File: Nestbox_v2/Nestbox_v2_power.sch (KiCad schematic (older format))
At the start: 24 parts, among them J201 BATT_CONN_01X02, U201 TPS62745, U202 LTC3534, U203 LP5907

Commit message: added stitching vias at power stage; reverse polarity protection and SD car enable mosfet
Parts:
- added Q201: Q_PMOS_DGS, Octanis3:TDSON-8-1_HandSoldering, symbol Q_PMOS_DGS
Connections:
- net +BATT: now also Q201.3 (S); no longer J201.2 (P2)
- net GND: now also U201.GND1 (GND), U201.GND2 (GND), Q201.2 (G)
- new net batt_in: J201.2 (P2), Q201.1 (D)
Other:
- moved on the sheet: J201
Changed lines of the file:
@@
 $EndComp
 $Comp
-L GND #PWR01
+L GND #PWR208
 U 1 1 5A0217A9
 P 3000 2550
-F 0 "#PWR01" H 3000 2300 50  0001 C CNN
+F 0 "#PWR208" H 3000 2300 50  0001 C CNN
 F 1 "GND" H 3005 2377 50  0000 C CNN
 F 2 "" H 3000 2550 50  0001 C CNN
@@
 $EndComp
 $Comp
-L GND #PWR02
+L GND #PWR203
 U 1 1 5A021A75
 P 1750 2400
-F 0 "#PWR02" H 1750 2150 50  0001 C CNN
+F 0 "#PWR203" H 1750 2150 50  0001 C CNN
 F 1 "GND" H 1755 2227 50  0000 C CNN
 F 2 "" H 1750 2400 50  0001 C CNN
@@
 $EndComp
 $Comp
-L +3.3V #PWR03
+L +3.3V #PWR219
 U 1 1 5A021DFB
 P 6750 1900
-F 0 "#PWR03" H 6750 1750 50  0001 C CNN
+F 0 "#PWR219" H 6750 1750 50  0001 C CNN
 F 1 "+3.3V" V 6765 2028 50  0000 L CNN
 F 2 "" H 6750 1900 50  0001 C CNN
@@
 $EndComp
 $Comp
-L GND #PWR04
+L GND #PWR209
 U 1 1 5A022A31
 P 3000 4850
-F 0 "#PWR04" H 3000 4600 50  0001 C CNN
+F 0 "#PWR209" H 3000 4600 50  0001 C CNN
 F 1 "GND" H 3005 4677 50  0000 C CNN
 F 2 "" H 3000 4850 50  0001 C CNN
@@
 $EndComp
 $Comp
-L GND #PWR05
+L GND #PWR205
 U 1 1 5A022A41
 P 2150 4650
-F 0 "#PWR05" H 2150 4400 50  0001 C CNN
+F 0 "#PWR205" H 2150 4400 50  0001 C CNN
 F 1 "GND" H 2155 4477 50  0000 C CNN
 F 2 "" H 2150 4650 50  0001 C CNN
@@
 $EndComp
 $Comp
-L +5V #PWR06
+L +5V #PWR220
 U 1 1 5A0232FE
 P 7600 4150
-F 0 "#PWR06" H 7600 4000 50  0001 C CNN
+F 0 "#PWR220" H 7600 4000 50  0001 C CNN
 F 1 "+5V" V 7615 4278 50  0000 L CNN
 F 2 "" H 7600 4150 50  0001 C CNN
@@
 $EndComp
 $Comp
-L GND #PWR07
+L GND #PWR218
 U 1 1 5A0246BF
 P 6500 4700
-F 0 "#PWR07" H 6500 4450 50  0001 C CNN
+F 0 "#PWR218" H 6500 4450 50  0001 C CNN
 F 1 "GND" H 6505 4527 50  0000 C CNN
 F 2 "" H 6500 4700 50  0001 C CNN
@@
 $EndComp
 $Comp
-L GND #PWR08
+L GND #PWR217
 U 1 1 5A0247CA
 P 5650 4800
-F 0 "#PWR08" H 5650 4550 50  0001 C CNN
+F 0 "#PWR217" H 5650 4550 50  0001 C CNN
 F 1 "GND" H 5655 4627 50  0000 C CNN
 F 2 "" H 5650 4800 50  0001 C CNN
@@
 $EndComp
 $Comp
-L GND #PWR09
+L GND #PWR216
 U 1 1 5A024E9A
 P 5300 2400
-F 0 "#PWR09" H 5300 2150 50  0001 C CNN
+F 0 "#PWR216" H 5300 2150 50  0001 C CNN
 F 1 "GND" H 5305 2227 50  0000 C CNN
 F 2 "" H 5300 2400 50  0001 C CNN
@@
 L CONN_01X02 J201
 U 1 1 5B072802
-P 8850 3200
-F 0 "J201" H 8850 3350 50  0000 C CNN
-F 1 "BATT_CONN_01X02" V 8950 3200 50  0000 C CNN
-F 2 "Terminal_Blocks:TerminalBlock_Pheonix_PT-3.5mm_2pol" H 8850 3200 50  0001 C CNN
-F 3 "" H 8850 3200 50  0001 C CNN
-	1    8850 3200
-	1    0    0    -1
-$EndComp
-$Comp
-L GND #PWR010
+P 9550 3200
+F 0 "J201" H 9550 3350 50  0000 C CNN
+F 1 "BATT_CONN_01X02" V 9650 3200 50  0000 C CNN
+F 2 "Terminal_Blocks:TerminalBlock_Pheonix_PT-3.5mm_2pol" H 9550 3200 50  0001 C CNN
+F 3 "" H 9550 3200 50  0001 C CNN
+	1    9550 3200
+	1    0    0    -1
+$EndComp
+$Comp
+L GND #PWR222
 U 1 1 5B072B3F
 P 8350 3150
-F 0 "#PWR010" H 8350 2900 50  0001 C CNN
+F 0 "#PWR222" H 8350 2900 50  0001 C CNN
 F 1 "GND" H 8350 3000 50  0000 C CNN
 F 2 "" H 8350 3150 50  0001 C CNN
@@
 $EndComp
 $Comp
-L +3V3 #PWR011
+L +3V3 #PWR204
 U 1 1 5B0757C4
 P 1950 6350
-F 0 "#PWR011" H 1950 6200 50  0001 C CNN
+F 0 "#PWR204" H 1950 6200 50  0001 C CNN
 F 1 "+3V3" H 1965 6523 50  0000 C CNN
 F 2 "" H 1950 6350 50  0001 C CNN
@@
 $EndComp
 $Comp
-L GND #PWR012
+L GND #PWR211
 U 1 1 5B0757CA
 P 3600 6800
-F 0 "#PWR012" H 3600 6550 50  0001 C CNN
+F 0 "#PWR211" H 3600 6550 50  0001 C CNN
 F 1 "GND" H 3605 6627 50  0000 C CNN
 F 2 "" H 3600 6800 50  0001 C CNN
@@
 NoConn ~ 4100 6450
 $Comp
-L VAA #PWR013
+L VAA #PWR215
 U 1 1 5B0757D1
 P 4700 5750
-F 0 "#PWR013" H 4700 5600 50  0001 C CNN
+F 0 "#PWR215" H 4700 5600 50  0001 C CNN
 F 1 "VAA" H 4717 5923 50  0000 C CNN
 F 2 "" H 4700 5750 50  0001 C CNN
@@
 $EndComp
 $Comp
-L +BATT #PWR014
+L +BATT #PWR201
 U 1 1 5B09033A
 P 700 1900
-F 0 "#PWR014" H 700 1750 50  0001 C CNN
+F 0 "#PWR201" H 700 1750 50  0001 C CNN
 F 1 "+BATT" H 700 2040 50  0000 C CNN
 F 2 "" H 700 1900 50  0001 C CNN
@@
 $EndComp
 $Comp
-L +BATT #PWR015
+L +BATT #PWR202
 U 1 1 5B090391
 P 1300 4150
-F 0 "#PWR015" H 1300 4000 50  0001 C CNN
+F 0 "#PWR202" H 1300 4000 50  0001 C CNN
 F 1 "+BATT" H 1300 4290 50  0000 C CNN
 F 2 "" H 1300 4150 50  0001 C CNN
@@
 $EndComp
 $Comp
-L GND #PWR016
+L GND #PWR207
 U 1 1 5B090D04
 P 2550 2950
-F 0 "#PWR016" H 2550 2700 50  0001 C CNN
+F 0 "#PWR207" H 2550 2700 50  0001 C CNN
 F 1 "GND" H 2555 2777 50  0000 C CNN
 F 2 "" H 2550 2950 50  0001 C CNN
@@
 $EndComp
 $Comp
-L GND #PWR017
+L GND #PWR206
 U 1 1 5B095296
 P 2500 6850
-F 0 "#PWR017" H 2500 6600 50  0001 C CNN
+F 0 "#PWR206" H 2500 6600 50  0001 C CNN
 F 1 "GND" H 2505 6677 50  0000 C CNN
 F 2 "" H 2500 6850 50  0001 C CNN
@@
 $EndComp
 $Comp
-L GND #PWR018
+L GND #PWR212
 U 1 1 5B095588
 P 4400 6800
-F 0 "#PWR018" H 4400 6550 50  0001 C CNN
+F 0 "#PWR212" H 4400 6550 50  0001 C CNN
 F 1 "GND" H 4405 6627 50  0000 C CNN
 F 2 "" H 4400 6800 50  0001 C CNN
@@
 $EndComp
 $Comp
-L +BATT #PWR019
+L +BATT #PWR221
 U 1 1 5B0B9A8C
 P 8200 3250
-F 0 "#PWR019" H 8200 3100 50  0001 C CNN
+F 0 "#PWR221" H 8200 3100 50  0001 C CNN
 F 1 "+BATT" H 8200 3390 50  0000 C CNN
 F 2 "" H 8200 3250 50  0001 C CNN
@@
 	2900 1900 2900 1700
 Wire Wire Line
-	8650 3150 8350 3150
-Wire Wire Line
-	8200 3250 8650 3250
+	8350 3150 8850 3150
+Wire Wire Line
+	8200 3250 8800 3250
 Wire Wire Line
 	1950 6350 3100 6350
@@
 Connection ~ 4550 4450
 $Comp
-L GND #PWR020
+L GND #PWR213
 U 1 1 5B11A0A6
 P 4500 4900
-F 0 "#PWR020" H 4500 4650 50  0001 C CNN
+F 0 "#PWR213" H 4500 4650 50  0001 C CNN
 F 1 "GND" H 4505 4727 50  0000 C CNN
 F 2 "" H 4500 4900 50  0001 C CNN
@@
 	3000 2400 3050 2400
 $Comp
-L +BATT #PWR021
+L +BATT #PWR214
 U 1 1 5B14A10E
 P 4550 2100
-F 0 "#PWR021" H 4550 1950 50  0001 C CNN
+F 0 "#PWR214" H 4550 1950 50  0001 C CNN
 F 1 "+BATT" H 4550 2240 50  0000 C CNN
 F 2 "" H 4550 2100 50  0001 C CNN
@@
 Wire Wire Line
 	4600 3800 4450 3800
-Connection ~ 8400 3250
 NoConn ~ 4450 1700
+Wire Wire Line
+	3500 2800 3500 2850
+Wire Wire Line
+	3500 2850 3600 2850
+Wire Wire Line
+	3600 2850 3600 2800
+$Comp
+L GND #PWR210
+U 1 1 5B18018D
+P 3500 2850
+F 0 "#PWR210" H 3500 2600 50  0001 C CNN
+F 1 "GND" H 3505 2677 50  0000 C CNN
+F 2 "" H 3500 2850 50  0001 C CNN
+F 3 "" H 3500 2850 50  0001 C CNN
+	1    3500 2850
+	1    0    0    -1
+$EndComp
+$Comp
+L Q_PMOS_DGS Q201
+U 1 1 5B18086E
+P 9000 3150
+F 0 "Q201" H 9200 3200 50  0000 L CNN
+F 1 "Q_PMOS_DGS" H 9200 3100 50  0000 L CNN
+F 2 "Octanis3:TDSON-8-1_HandSoldering" H 9200 3250 50  0001 C CNN
+F 3 "" H 9000 3150 50  0001 C CNN
+	1    9000 3150
+	0    1    1    0
+$EndComp
+Wire Wire Line
+	9200 3250 9350 3250
+Wire Wire Line
+	8850 3150 8850 2900
+Wire Wire Line
+	8850 2900 9250 2900
+Wire Wire Line
+	9250 2900 9250 3150
+Wire Wire Line
+	9250 3150 9350 3150
+Wire Wire Line
+	9000 2950 9000 2900
+Connection ~ 9000 2900
+Text Label 9200 3250 0    60   ~ 0
+batt_in
 $EndSCHEMATC

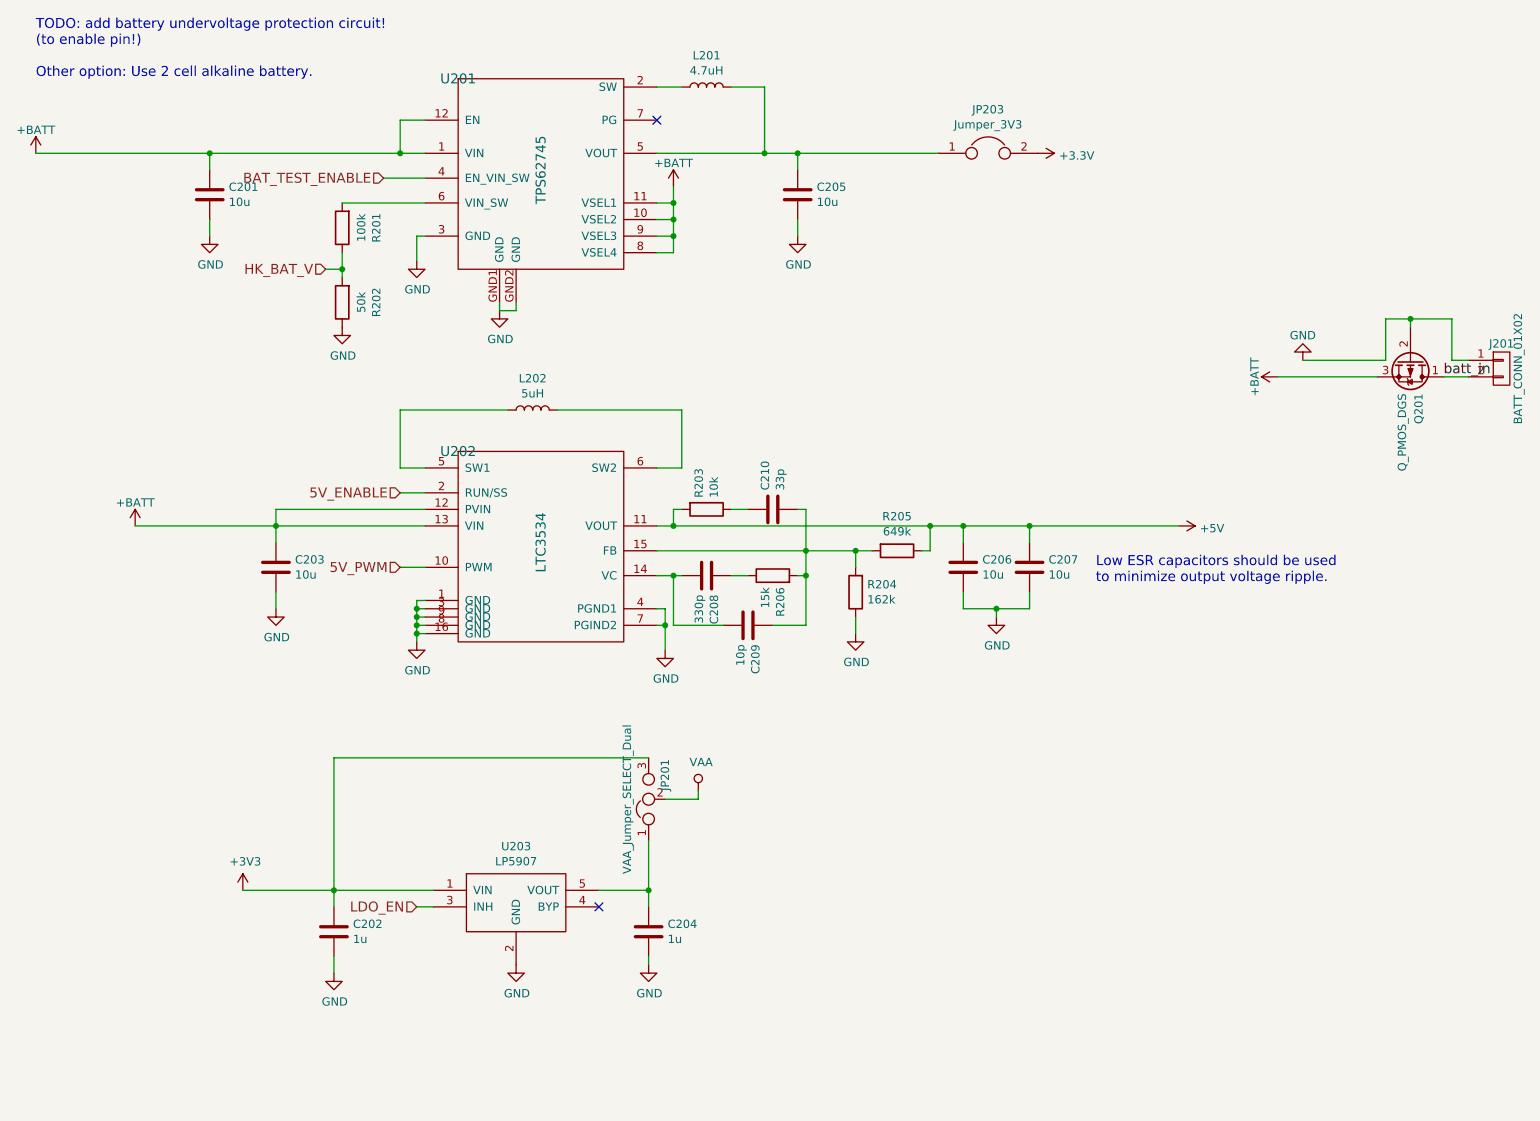
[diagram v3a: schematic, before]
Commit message: annotated schematic with necessary changes to load cell circuit. added pull-ups for enable PMOSes
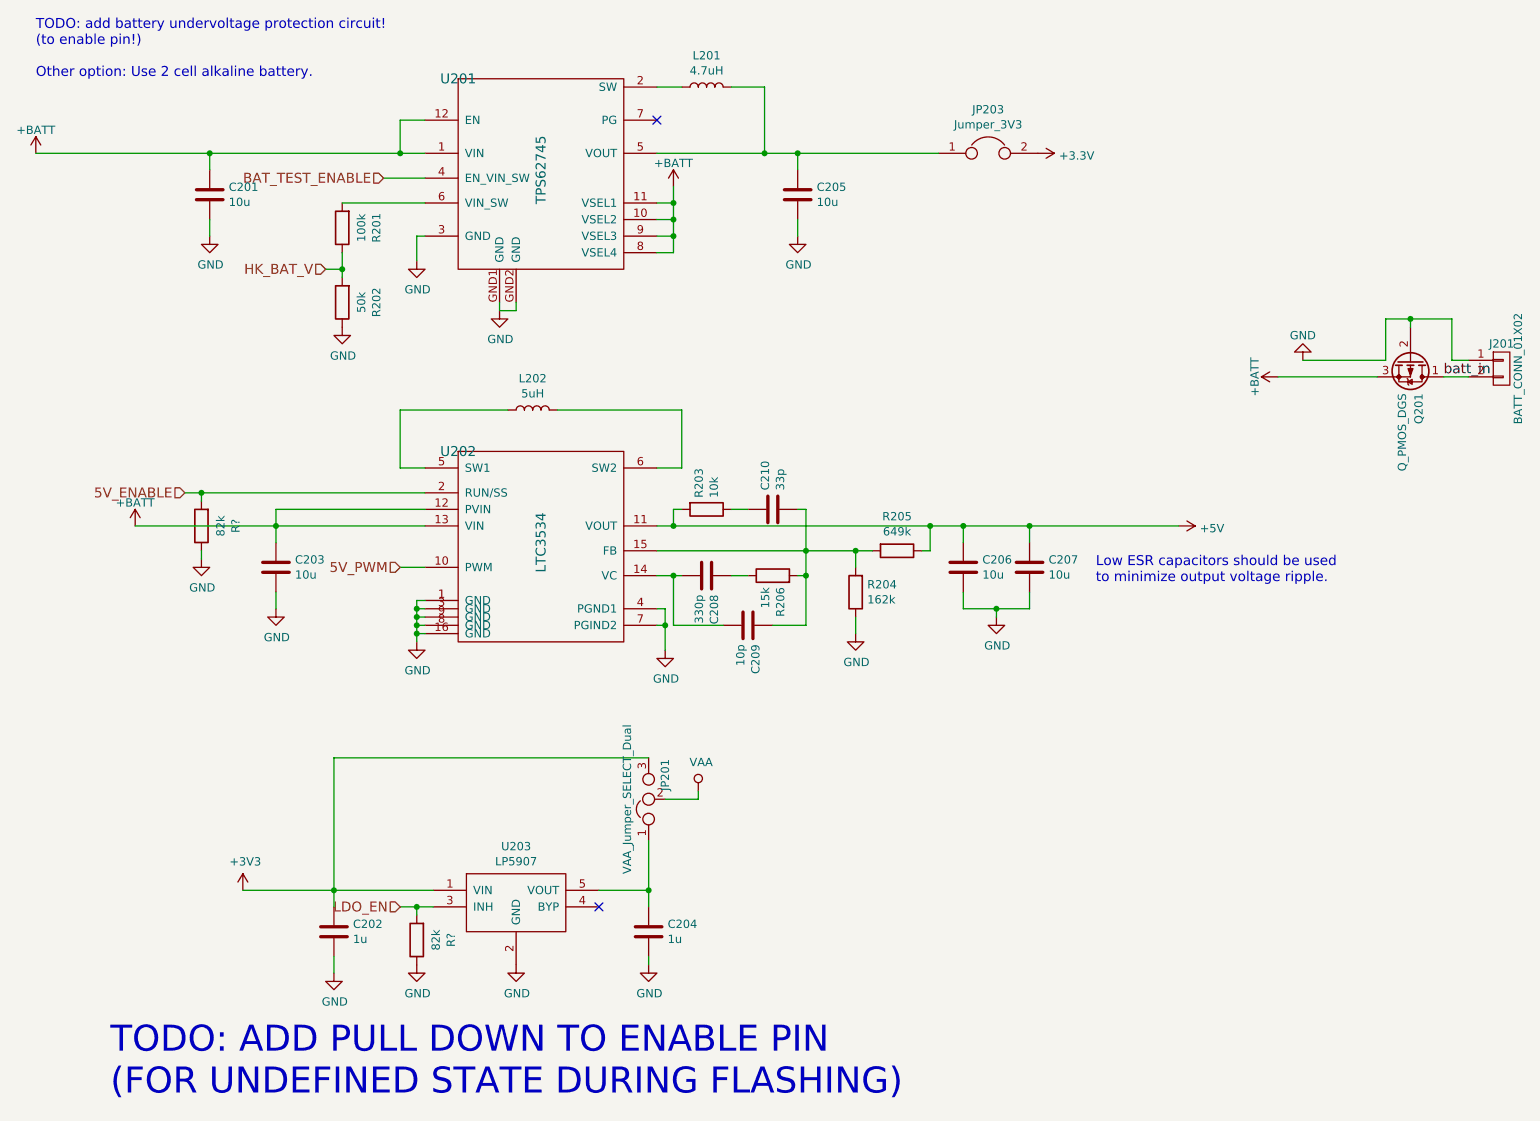
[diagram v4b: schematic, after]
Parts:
- added R? (x2): 82k, Resistors_SMD:R_0603, symbol R
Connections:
- net 5V_ENABLE: now also R?.2
- net GND: now also R?.1, R?.1
- net LDO_EN: now also R?.2
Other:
- note added: "TODO: ADD PULL DOWN TO ENABLE PIN \n(FOR UNDEFINED STATE DURING FLASHING)"
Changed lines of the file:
@@
 	1    0    0    -1
 $EndComp
-Text HLabel 2900 3950 0    60   Input ~ 0
+Text HLabel 1600 3950 0    60   Input ~ 0
 5V_ENABLE
 Text HLabel 2450 2600 0    60   Input ~ 0
@@
 	1    0    0    -1
 $EndComp
-Text HLabel 3000 6450 0    60   Input ~ 0
+Text HLabel 2900 6450 0    60   Input ~ 0
 LDO_EN
 $Comp
@@
 	1950 6350 3100 6350
 Wire Wire Line
-	3100 6450 3000 6450
+	3100 6450 2900 6450
 Wire Wire Line
 	4100 6350 4400 6350
@@
 	2900 3800 3050 3800
 Wire Wire Line
-	3050 3950 2900 3950
+	1600 3950 3050 3950
 Wire Wire Line
 	3050 4050 2150 4050
@@
 Text Label 9200 3250 0    60   ~ 0
 batt_in
+Text Notes 1150 7600 0    157  ~ 0
+TODO: ADD PULL DOWN TO ENABLE PIN \n(FOR UNDEFINED STATE DURING FLASHING)
+$Comp
+L R R?
+U 1 1 5B28CE2A
+P 1700 4150
+F 0 "R?" V 1493 4150 50  0000 C CNN
+F 1 "82k" V 1584 4150 50  0000 C CNN
+F 2 "Resistors_SMD:R_0603" V 1630 4150 50  0001 C CNN
+F 3 "" H 1700 4150 50  0001 C CNN
+	1    1700 4150
+	-1   0    0    1
+$EndComp
+Wire Wire Line
+	1700 4000 1700 3950
+Connection ~ 1700 3950
+$Comp
+L GND #PWR?
+U 1 1 5B28CF96
+P 1700 4350
+F 0 "#PWR?" H 1700 4100 50  0001 C CNN
+F 1 "GND" H 1705 4177 50  0000 C CNN
+F 2 "" H 1700 4350 50  0001 C CNN
+F 3 "" H 1700 4350 50  0001 C CNN
+	1    1700 4350
+	1    0    0    -1
+$EndComp
+Wire Wire Line
+	1700 4350 1700 4300
+$Comp
+L R R?
+U 1 1 5B28D28A
+P 3000 6650
+F 0 "R?" V 2793 6650 50  0000 C CNN
+F 1 "82k" V 2884 6650 50  0000 C CNN
+F 2 "Resistors_SMD:R_0603" V 2930 6650 50  0001 C CNN
+F 3 "" H 3000 6650 50  0001 C CNN
+	1    3000 6650
+	-1   0    0    1
+$EndComp
+Wire Wire Line
+	3000 6500 3000 6450
+Connection ~ 3000 6450
+$Comp
+L GND #PWR?
+U 1 1 5B28D3DF
+P 3000 6800
+F 0 "#PWR?" H 3000 6550 50  0001 C CNN
+F 1 "GND" H 3005 6627 50  0000 C CNN
+F 2 "" H 3000 6800 50  0001 C CNN
+F 3 "" H 3000 6800 50  0001 C CNN
+	1    3000 6800
+	1    0    0    -1
+$EndComp
 $EndSCHEMATC
